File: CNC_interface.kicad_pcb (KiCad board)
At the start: 2 copper layers, 38 parts, among them J1 Conn_01x04_Male, J10 Conn_01x08, J11 Conn_01x08, J12 Conn_01x08, J13 Conn_01x08, J14 Conn_01x03_Male, J15 Conn_01x03_Male, J16 Conn_01x03_Male, J17 Conn_01x08, J18 Conn_01x10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

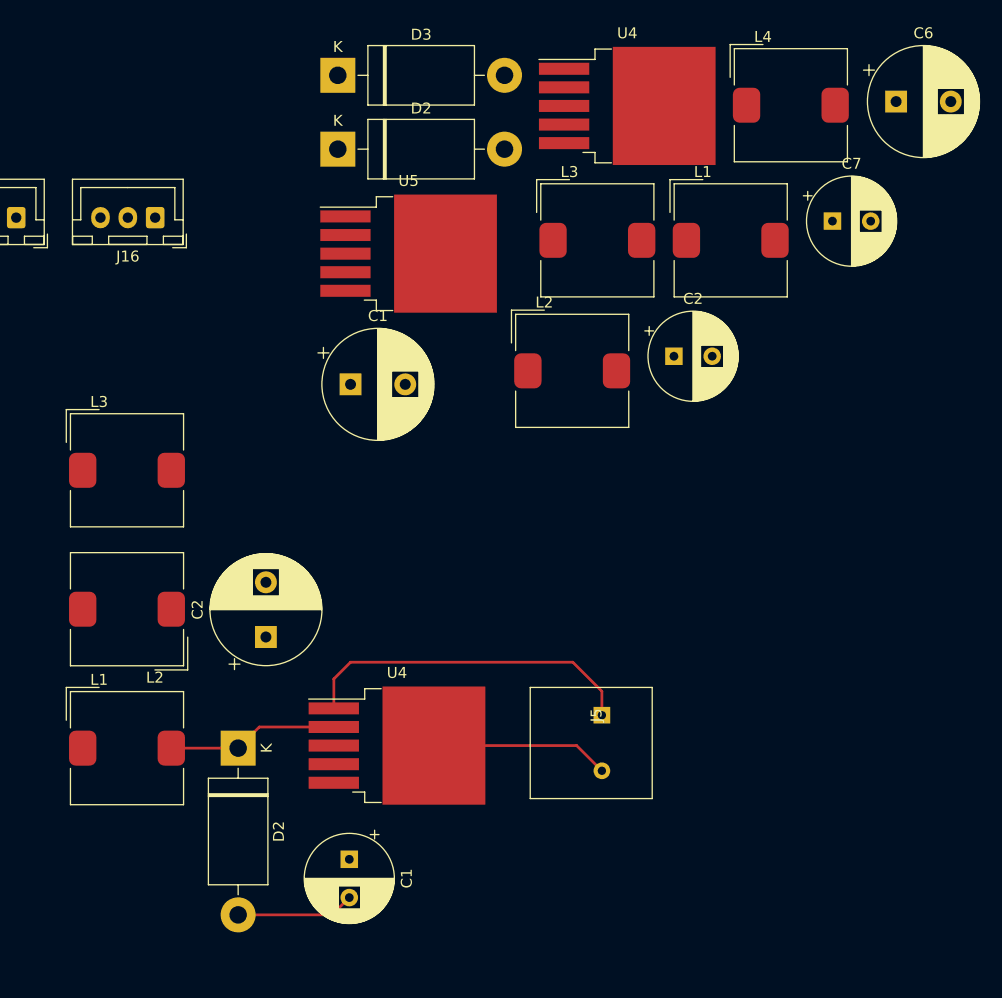
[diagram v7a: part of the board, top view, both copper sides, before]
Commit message: delete the short circuit
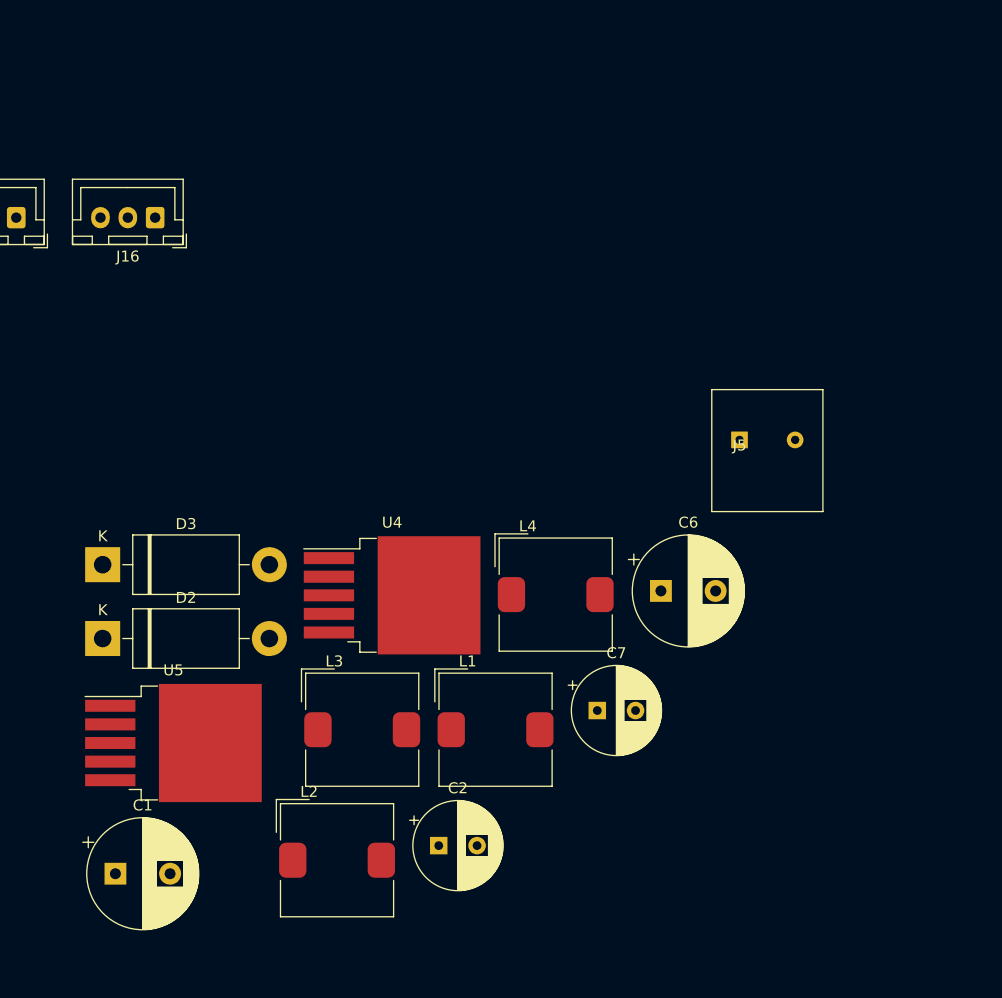
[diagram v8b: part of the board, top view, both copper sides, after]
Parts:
- removed the C1 at (129.4, 94.2)
- removed the C2 at (121.8, 73.9)
- removed the D2 at (119.3, 84.1)
- removed the L1 at (109.1, 84.1)
- removed the L2 at (109.1, 71.4)
- removed the L3 at (109.1, 58.7)
- removed the U4 at (133.8, 83.8)
- moved L1 49.6 mm to (142.8, 82.4)
- moved L3 49.6 mm to (130.6, 82.4)
- moved C2 49.6 mm to (137.6, 93.0)
- moved L4 49.6 mm to (148.3, 70.0)
- moved C1 49.6 mm to (108.0, 95.5)
- moved C6 49.6 mm to (157.9, 69.7)
- moved D2 49.6 mm to (106.9, 74.0)
- moved D3 49.6 mm to (106.9, 67.3)
- moved L2 49.6 mm to (128.3, 94.3)
- moved C7 49.6 mm to (152.1, 80.6)
- moved U4 49.6 mm to (133.3, 70.1)
- moved U5 49.6 mm to (113.3, 83.6)
- moved J5 28.1 mm to (165.1, 55.9), turned to 0 degrees
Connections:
- C1 pad 2: +5V -> GND
- C2 pad 2: +5V -> GND
- C6 pad 2: +5V -> GND
- C7 pad 2: +5V -> GND
- D2 pad 2: +5V -> GND
- D3 pad 2: +5V -> GND
- J10 pad 1: +5V -> GND
- J10 pad 7: +5V -> GND
- J12 pad 1: +5V -> GND
- J12 pad 7: +5V -> GND
- J14 pad 2: +5V -> GND
- J15 pad 2: +5V -> GND
- J16 pad 2: +5V -> GND
- J18 pad 4: +5V -> GND
- J19 pad A1: +5V -> GND
- J19 pad A12: +5V -> GND
- J19 pad B1: +5V -> GND
- J19 pad B12: +5V -> GND
- J19 pad S1: +5V -> GND
- J5 pad 2: +5V -> GND
- J8 pad 1: +5V -> GND
- J8 pad 7: +5V -> GND
- Q1 pad 3: +5V -> GND
- U4 pad 3: +5V -> GND
- U4 pad 5: +5V -> GND
- U5 pad 3: +5V -> GND
- U5 pad 5: +5V -> GND
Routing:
- net +24V: track 31.1 -> 0.00 mm
- net +5V: track 16.3 -> 0.00 mm
- net Net-(D2-Pad1) (its old number): track 15.7 -> 0.00 mm
- net GND: track 10.8 -> 0.00 mm
